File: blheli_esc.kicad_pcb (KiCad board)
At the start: 2 copper layers, 45 parts, among them J1 Conn_01x03_Male, Q1 BC847, Q2 BC847, Q3 BC847, U1 AP1509, U2 EFM8BB21F16G

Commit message: first draft complete
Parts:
- C1, C2, C3: moved to B.Cu
- J1: footprint Connector:FanPinHeader_1x03_P2.54mm_Vertical -> Connector_PinHeader_2.54mm:PinHeader_1x03_P2.54mm_Vertical
- L1: footprint Inductor_SMD:L_12x12mm_H4.5mm -> blheli_esc:inductor_3x3mm
- moved TP1 66.2 mm to (152.4, 72.9)
- moved TP3 39.6 mm to (155.4, 74.7)
- moved TP5 37.2 mm to (152.4, 70.9)
- moved TP2 32.0 mm to (153.4, 74.7)
- moved L1 25.0 mm to (155.6, 78.2)
- moved D1 18.1 mm to (151.5, 76.8), turned to 180 degrees
- moved TP4 12.3 mm to (152.4, 67.3)
- moved C1 5.42 mm to (154.4, 79.8)
- moved C5 4.35 mm to (153.0, 79.5), turned to 90 degrees
- moved C7 4.35 mm to (151.5, 79.5), turned to 90 degrees
- moved PAD2 3.88 mm to (148.6, 77.2)
- moved C2 2.95 mm to (152.9, 79.8)
- moved PAD1 2.70 mm to (148.6, 81.3)
- moved C3 2.41 mm to (151.4, 79.8)
- moved J1 0.15 mm to (148.9, 68.3), turned to 0 degrees
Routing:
- net GND: track 4.62 -> 39.1 mm, vias 0 -> 11
- net C_SENSE: track 2.75 -> 29.9 mm
- net B_SENSE: track 2.01 -> 23.9 mm, vias 0 -> 2
- net 3V3: track 4.11 -> 24.1 mm
- net CP: track 0.00 -> 19.7 mm
- net AP: track 0.00 -> 19.4 mm
- net BP: track 0.00 -> 17.0 mm
- net A_SENSE: track 2.65 -> 18.5 mm, vias 0 -> 2
- net TX2: track 2.21 -> 11.6 mm
- net Net-(D1-Pad1): track 0.00 -> 7.53 mm
- net CC: track 0.00 -> 7.13 mm
- net AC: track 0.00 -> 5.75 mm
- net Net-(J1-Pad2): track 0.00 -> 4.61 mm
- net BC: track 0.00 -> 3.53 mm
- net RC_IN: track 15.6 -> 19.1 mm
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- added copper zone on B.Cu, net GND
- added copper zone on B.Cu, net V_BATT
- added copper zone on F.Cu, net V_BATT
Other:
- board outline added: 33 x 17.8 mm

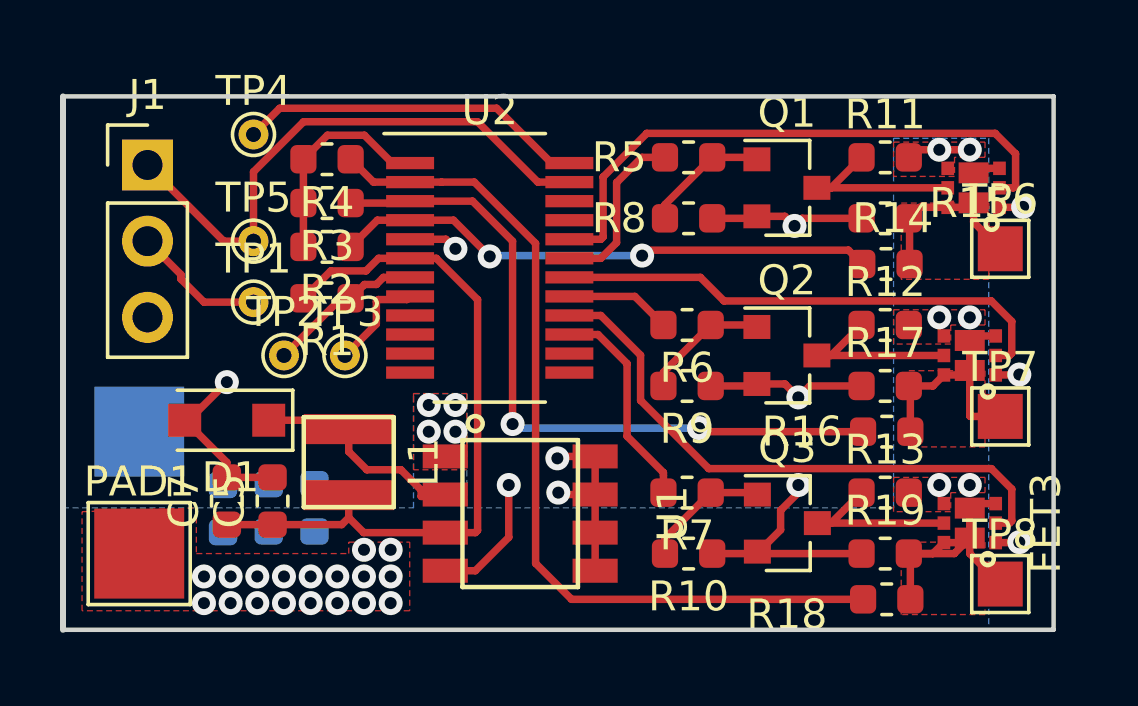
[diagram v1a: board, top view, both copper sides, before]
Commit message: finished layout with moved vbatt
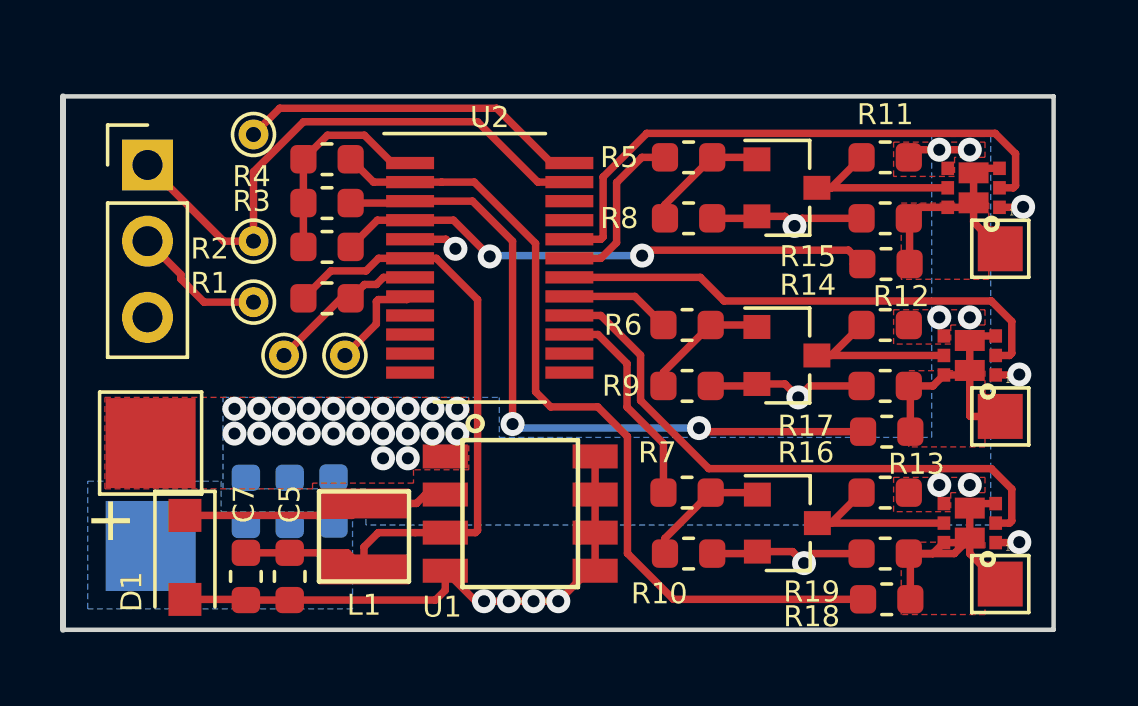
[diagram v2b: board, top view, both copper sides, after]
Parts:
- moved D1 4.78 mm to (150.1, 81.4), turned to 270 degrees
- moved PAD2 3.83 mm to (149.0, 81.0)
- moved PAD1 3.70 mm to (149.0, 77.6)
- moved C7 2.59 mm to (152.1, 82.0), turned to 270 degrees
- moved C5 2.58 mm to (153.6, 82.0), turned to 270 degrees
- moved L1 2.53 mm to (156.1, 80.7)
- moved C3 0.80 mm to (152.1, 79.5), turned to 270 degrees
- moved C2 0.73 mm to (153.6, 79.5), turned to 270 degrees
- moved C1 0.67 mm to (155.1, 79.5), turned to 270 degrees
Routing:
- net Net-(D1-Pad1): track 7.53 -> 8.97 mm
- net C_SENSE: track 29.9 -> 28.8 mm
- net 3V3: track 24.1 -> 23.6 mm
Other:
- board text added: "+"
- board text added: "-"
- board text added: "1"
- board text added: "2S MAX INPUT"
- board text added: "C2CK"
- board text added: "C2D"
- board text added: "EITAN BABCOCK BLHELI ESC V1.0"
- board text added: "RC_IN"
- board text added: "SERVO_P2"
- board text added: "TX"

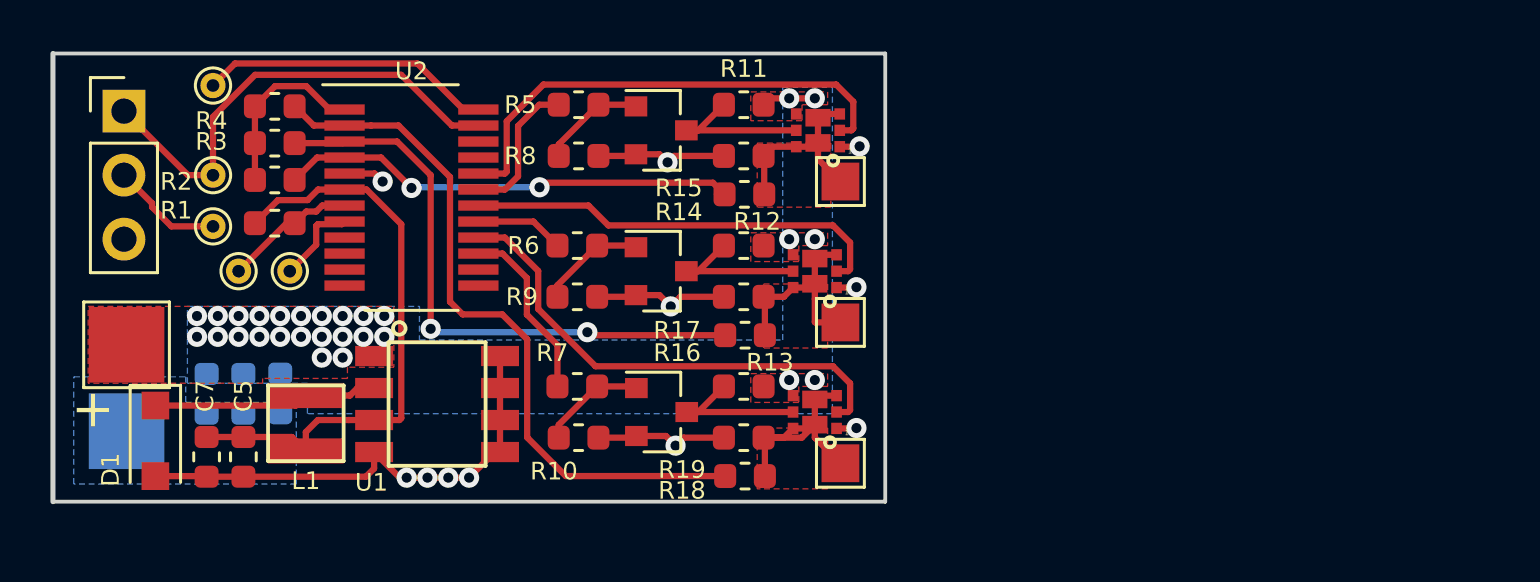
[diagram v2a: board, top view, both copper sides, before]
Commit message: new design with easier to solder fets. 4 layer board
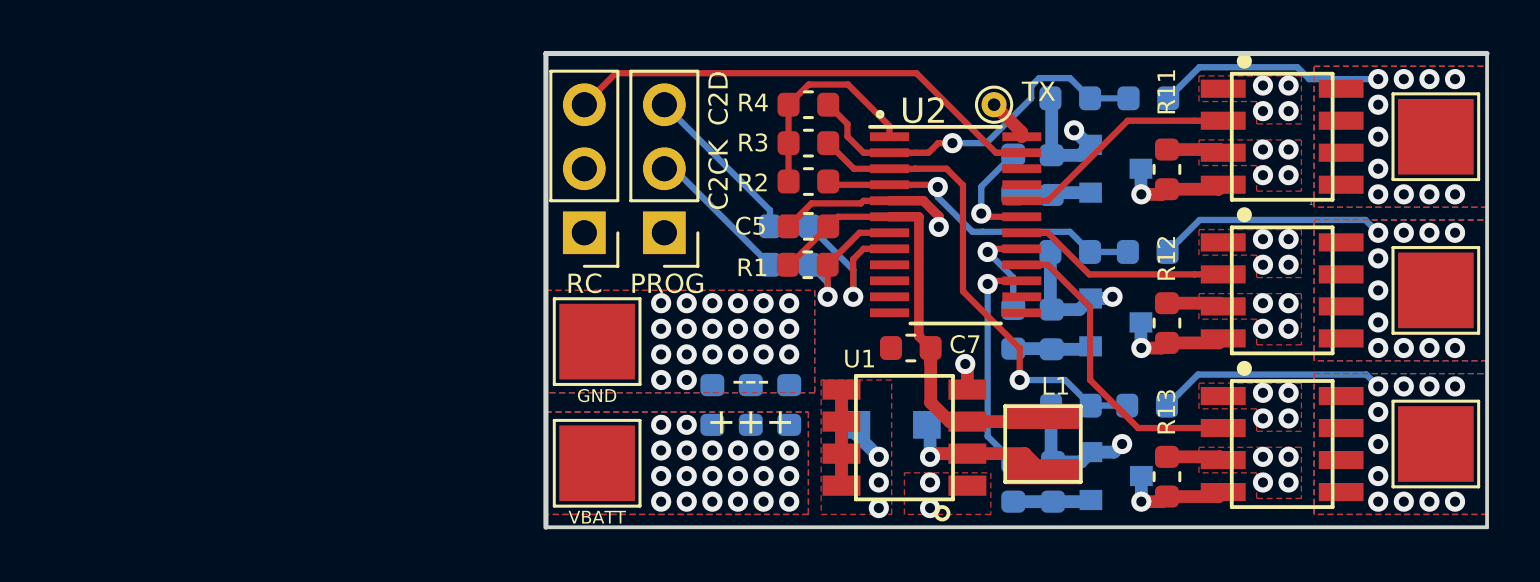
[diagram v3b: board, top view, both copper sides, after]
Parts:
- removed FET1, FET2, FET3: UT6MA3, blheli_esc:UT6MA3
- removed TP1: SERVO_TP, TestPoint:TestPoint_THTPad_D1.0mm_Drill0.5mm
- removed TP2: C2CK, TestPoint:TestPoint_THTPad_D1.0mm_Drill0.5mm
- removed TP3: C2D, TestPoint:TestPoint_THTPad_D1.0mm_Drill0.5mm
- removed TP5: RC_IN, TestPoint:TestPoint_THTPad_D1.0mm_Drill0.5mm
- added J2: Conn_01x03_Male, Connector_PinHeader_2.54mm:PinHeader_1x03_P2.54mm_Vertical, F.Cu at (170.3, 73.2)
- added R20: 0, Resistor_SMD:R_0603_1608Metric, B.Cu at (175.3, 74.4)
- added R21: 0, Resistor_SMD:R_0603_1608Metric, B.Cu at (175.3, 72.9)
- added U3: IRF73xx, blheli_esc:IRF7317PbF, F.Cu at (194.8, 69.3)
- added U4: IRF73xx, blheli_esc:IRF7317PbF, F.Cu at (194.8, 75.4)
- added U5: IRF73xx, blheli_esc:IRF7317PbF, F.Cu at (194.8, 81.5)
- C5: value 100n -> 22u
- D1, Q1, Q2, Q3, R10, R14, R15, R16, R17, R18, R19, R5, R6, R7, R8, R9: moved to B.Cu
- PAD2: moved to F.Cu
- TP6, TP7, TP8: footprint TestPoint:TestPoint_Pad_1.5x1.5mm -> TestPoint:TestPoint_Pad_3.0x3.0mm
- U2: footprint Package_SO:QSOP-24_3.9x8.7mm_P0.635mm -> blheli_esc:efm8b21-qsop24
- moved TP4 31.0 mm to (183.4, 68.1)
- moved L1 29.3 mm to (185.3, 81.5), turned to 270 degrees
- moved D1 29.2 mm to (179.3, 80.8), turned to 180 degrees
- moved C7 28.3 mm to (180.1, 77.7), turned to 180 degrees
- moved C5 24.2 mm to (176.0, 72.9), turned to 180 degrees
- moved TP6 23.7 mm to (200.9, 69.3)
- moved TP7 23.7 mm to (200.9, 75.4)
- moved TP8 23.6 mm to (200.9, 81.5)
- moved U2 21.6 mm to (181.9, 73.2)
- moved R1 21.2 mm to (176.0, 74.4)
- moved R2 21.2 mm to (176.0, 71.1)
- moved R4 21.2 mm to (176.0, 68.1)
- moved R3 21.2 mm to (176.0, 69.6)
- moved C1 20.2 mm to (175.3, 80.0), turned to 90 degrees
- moved C2 20.1 mm to (173.7, 80.0), turned to 90 degrees
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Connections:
- J1 pad 1: RC_IN -> GND
- J1 pad 2: Net-(J1-Pad2) -> (no net)
- J1 pad 3: GND -> RC_IN
- R14 pad 1: PHASE_A -> A_SENSE
- R14 pad 2: A_SENSE -> PHASE_A
- R15 pad 2: PHASE_A -> A_SENSE
- R16 pad 1: PHASE_B -> B_SENSE
- R16 pad 2: B_SENSE -> PHASE_B
- R17 pad 2: PHASE_B -> B_SENSE
- R18 pad 1: PHASE_C -> C_SENSE
- R18 pad 2: C_SENSE -> PHASE_C
- R19 pad 2: PHASE_C -> C_SENSE
- R2 pad 1: A_SENSE -> B_SENSE
- R3 pad 1: B_SENSE -> C_SENSE
- R4 pad 1: C_SENSE -> A_SENSE
- U2 pad 2: C_SENSE -> A_SENSE
- U2 pad 3: B_SENSE -> C_SENSE
- U2 pad 4: A_SENSE -> B_SENSE
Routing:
- net B_SENSE: track 23.9 -> 13.3 mm, vias 2 -> 1
- net GND: track 39.1 -> 28.7 mm, vias 11 -> 40
- net AP: track 19.4 -> 9.30 mm
- net TX2: track 11.6 -> 1.73 mm
- net C_SENSE: track 28.8 -> 19.4 mm, vias 0 -> 1
- net BP: track 17.0 -> 8.67 mm
- net CP: track 19.7 -> 12.4 mm
- net Net-(J2-Pad3): track 0.00 -> 6.86 mm
- net Net-(J2-Pad2): track 0.00 -> 5.77 mm
- net 3V3: track 23.6 -> 18.4 mm
- net V_BATT: track 2.14 -> 6.85 mm, vias 28 -> 34
- net Net-(J1-Pad2): track 4.61 -> 0.00 mm
- net A_SENSE: track 18.5 -> 14.8 mm, vias 2 -> 1
- net C2D: track 3.43 -> 6.61 mm, vias 0 -> 1
- net Net-(D1-Pad1): track 8.97 -> 6.15 mm, vias 0 -> 1
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- added copper zone on F.Cu, net GND
- added copper zone on In1.Cu, net GND
- added copper zone on B.Cu, net PHASE_A
- added copper zone on In1.Cu, net PHASE_A
- added copper zone on In2.Cu, net PHASE_A
- added copper zone on B.Cu, net PHASE_B
- added copper zone on In1.Cu, net PHASE_B
- added copper zone on In2.Cu, net PHASE_B
- added copper zone on B.Cu, net PHASE_C
- added copper zone on In1.Cu, net PHASE_C
- added copper zone on In2.Cu, net PHASE_C
- added copper zone on In2.Cu, net V_BATT
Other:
- board size 33 x 17.8 mm -> 37.3 x 18.8 mm
- copper layers 2 -> 4
- board text added: "+++"
- board text added: "---"
- board text added: "EITAN BABCOCK BLHELI ESC V2.0"
- board text added: "GND"
- board text added: "PROG"
- board text added: "RC"
- board text added: "VBATT"
- board text removed: "+"
- board text removed: "-"
- board text removed: "EITAN BABCOCK BLHELI ESC V1.0"
- board text removed: "RC_IN"
- board text removed: "SERVO_P2"

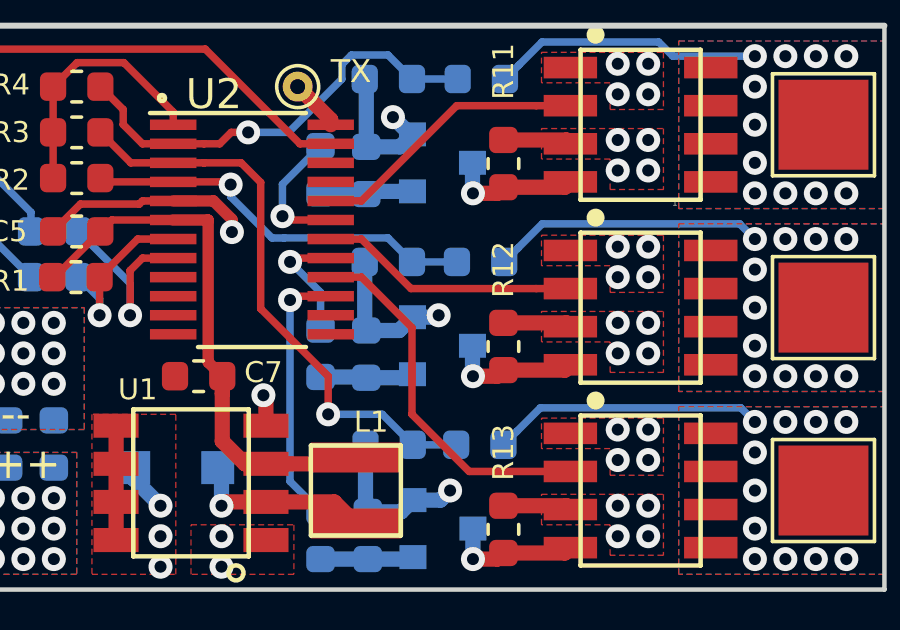
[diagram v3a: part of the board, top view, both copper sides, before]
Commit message: small tweaks to layout
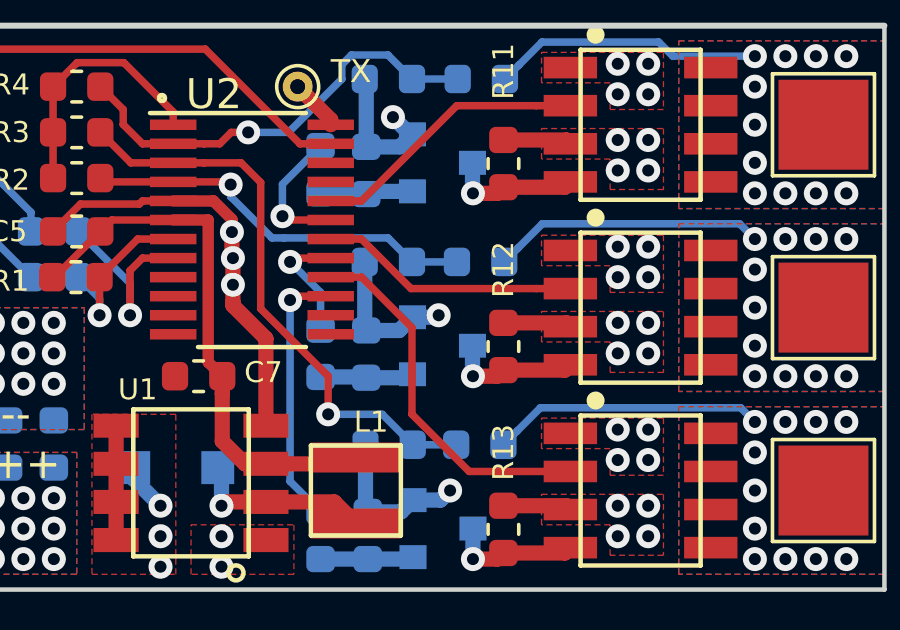
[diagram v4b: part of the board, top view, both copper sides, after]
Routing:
- net GND: track 28.7 -> 34.6 mm, vias 40 -> 41
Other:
- board text removed: "1"
